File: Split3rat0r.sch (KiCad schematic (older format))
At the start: 69 parts, among them J1 Conn_01x20, K1 KEYSW, K10 KEYSW, K11 KEYSW, K12 KEYSW, K13 KEYSW, K14 KEYSW, K15 KEYSW, K16 KEYSW, K17 KEYSW, K18 KEYSW, K19 KEYSW, K2 KEYSW, K20 KEYSW, K21 KEYSW, K22 KEYSW, K23 KEYSW, K24 KEYSW, K25 KEYSW, K26 KEYSW, K27 KEYSW, K28 KEYSW, K29 KEYSW, K3 KEYSW, K30 KEYSW, K4 KEYSW, K5 KEYSW, K6 KEYSW, K7 KEYSW, K8 KEYSW, K9 KEYSW, U1 TEENSY2.0

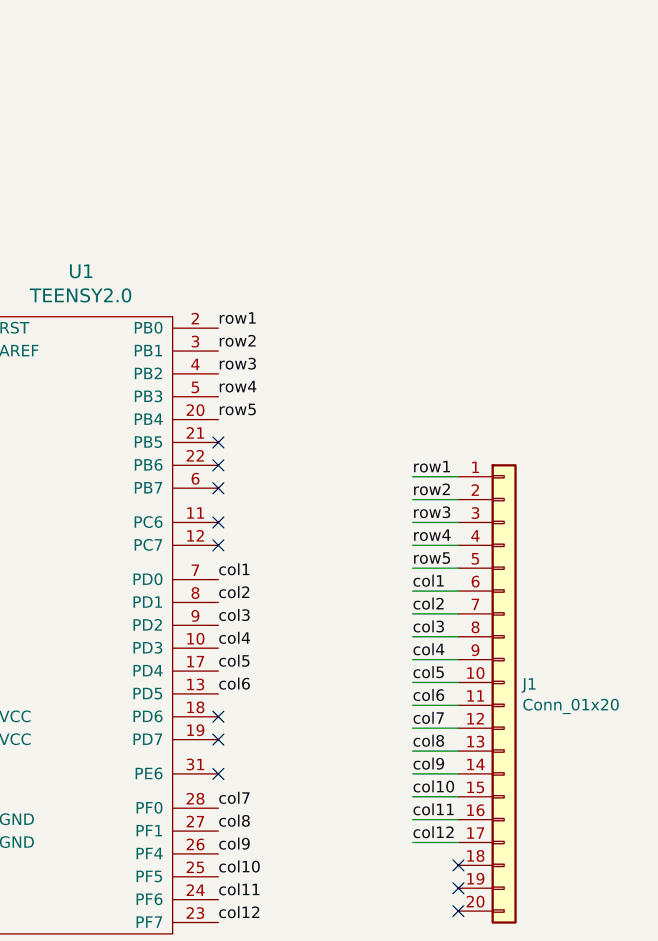
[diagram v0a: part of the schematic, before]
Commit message: Added LEDs beginning pcb layout
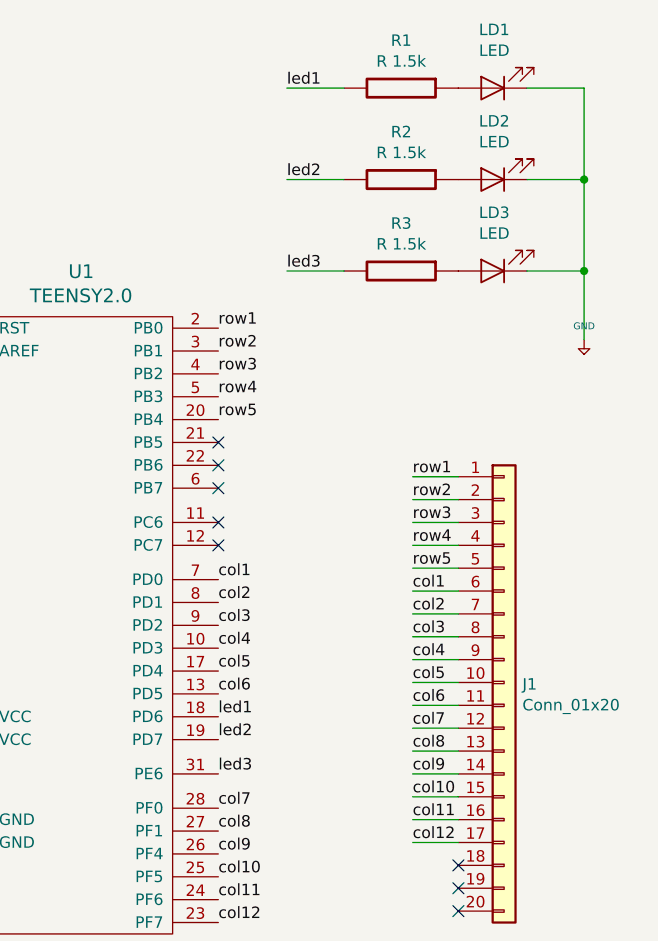
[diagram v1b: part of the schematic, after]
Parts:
- added LD1, LD2, LD3: LED, keeb_parts:LED_TH, symbol Device:LED
- added R1, R2, R3: R 1.5k, Resistor_THT:R_Axial_DIN0204_L3.6mm_D1.6mm_P5.08mm_Horizontal, symbol keeb_parts:R
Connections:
- net +5V: now also LD1.1 (K), LD2.1 (K), LD3.1 (K)
- net led1: now reaches U1.18 (PD6)
- net led1: now also R1.2
- net led2: now reaches U1.19 (PD7)
- net led2: now also R2.2
- net led3: now reaches U1.31 (PE6)
- net led3: now also R3.2
- new net: LD1.2 (A), R1.1
- new net: LD2.2 (A), R2.1
- new net: LD3.2 (A), R3.1
- no-connect marks 13 -> 10
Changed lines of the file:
@@
 NoConn ~ 8900 2850
 NoConn ~ 8900 2950
-NoConn ~ 8900 3700
-NoConn ~ 8900 3800
-NoConn ~ 8900 3950
 NoConn ~ 9950 4350
 NoConn ~ 9950 4450
@@
 	1    0    0    -1
 $EndComp
+$Comp
+L Device:LED LD1
+U 1 1 5CD186EE
+P 10100 950
+F 0 "LD1" H 10093 695 50  0000 C CNN
+F 1 "LED" H 10093 786 50  0000 C CNN
+F 2 "keeb_parts:LED_TH" H 10100 950 50  0001 C CNN
+F 3 "~" H 10100 950 50  0001 C CNN
+	1    10100 950
+	-1   0    0    1
+$EndComp
+$Comp
+L Device:LED LD2
+U 1 1 5CD19CA1
+P 10100 1350
+F 0 "LD2" H 10093 1095 50  0000 C CNN
+F 1 "LED" H 10093 1186 50  0000 C CNN
+F 2 "keeb_parts:LED_TH" H 10100 1350 50  0001 C CNN
+F 3 "~" H 10100 1350 50  0001 C CNN
+	1    10100 1350
+	-1   0    0    1
+$EndComp
+$Comp
+L Device:LED LD3
+U 1 1 5CD19E40
+P 10100 1750
+F 0 "LD3" H 10093 1495 50  0000 C CNN
+F 1 "LED" H 10093 1586 50  0000 C CNN
+F 2 "keeb_parts:LED_TH" H 10100 1750 50  0001 C CNN
+F 3 "~" H 10100 1750 50  0001 C CNN
+	1    10100 1750
+	-1   0    0    1
+$EndComp
+$Comp
+L keeb_parts:GND #PWR0105
+U 1 1 5CD1D128
+P 10500 2050
+F 0 "#PWR0105" H 10500 2100 20  0001 C CNN
+F 1 "GND" H 10500 2109 30  0000 C CNN
+F 2 "" H 10500 2050 60  0000 C CNN
+F 3 "" H 10500 2050 60  0000 C CNN
+	1    10500 2050
+	1    0    0    -1
+$EndComp
+Wire Wire Line
+	10250 1750 10500 1750
+Wire Wire Line
+	10500 1350 10250 1350
+Wire Wire Line
+	10250 950  10500 950
+Text Label 9200 950  0    50   ~ 0
+led1
+Text Label 9200 1350 0    50   ~ 0
+led2
+Text Label 9200 1750 0    50   ~ 0
+led3
+$Comp
+L keeb_parts:R R1
+U 1 1 5CD54691
+P 9700 950
+F 0 "R1" V 9492 950 50  0000 C CNN
+F 1 "R 1.5k" V 9583 950 50  0000 C CNN
+F 2 "Resistor_THT:R_Axial_DIN0204_L3.6mm_D1.6mm_P5.08mm_Horizontal" H 9700 950 60  0001 C CNN
+F 3 "" H 9700 950 60  0000 C CNN
+	1    9700 950
+	0    1    1    0
+$EndComp
+$Comp
+L keeb_parts:R R2
+U 1 1 5CD55293
+P 9700 1350
+F 0 "R2" V 9492 1350 50  0000 C CNN
+F 1 "R 1.5k" V 9583 1350 50  0000 C CNN
+F 2 "Resistor_THT:R_Axial_DIN0204_L3.6mm_D1.6mm_P5.08mm_Horizontal" H 9700 1350 60  0001 C CNN
+F 3 "" H 9700 1350 60  0000 C CNN
+	1    9700 1350
+	0    1    1    0
+$EndComp
+$Comp
+L keeb_parts:R R3
+U 1 1 5CD55692
+P 9700 1750
+F 0 "R3" V 9492 1750 50  0000 C CNN
+F 1 "R 1.5k" V 9583 1750 50  0000 C CNN
+F 2 "Resistor_THT:R_Axial_DIN0204_L3.6mm_D1.6mm_P5.08mm_Horizontal" H 9700 1750 60  0001 C CNN
+F 3 "" H 9700 1750 60  0000 C CNN
+	1    9700 1750
+	0    1    1    0
+$EndComp
+Wire Wire Line
+	9200 950  9450 950
+Wire Wire Line
+	9450 1350 9200 1350
+Wire Wire Line
+	9200 1750 9450 1750
+Wire Wire Line
+	10500 950  10500 1350
+Connection ~ 10500 1750
+Connection ~ 10500 1350
+Wire Wire Line
+	10500 1350 10500 1750
+Wire Wire Line
+	10500 1750 10500 2050
+Text Label 8900 3700 0    50   ~ 0
+led1
+Text Label 8900 3800 0    50   ~ 0
+led2
+Text Label 8900 3950 0    50   ~ 0
+led3
 $EndSCHEMATC

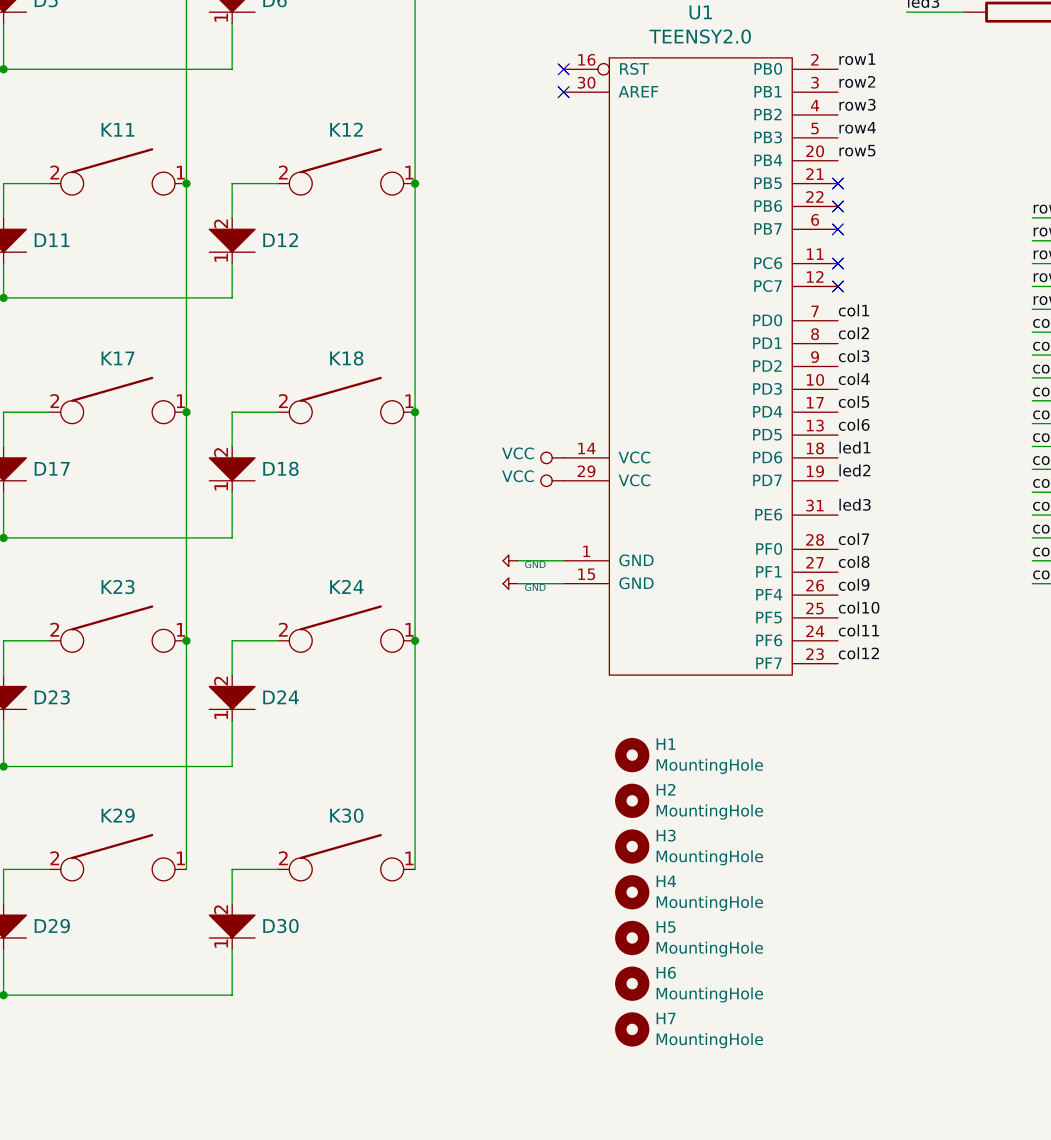
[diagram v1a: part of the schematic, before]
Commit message: Added rotary acoder switch + pcb layout progress
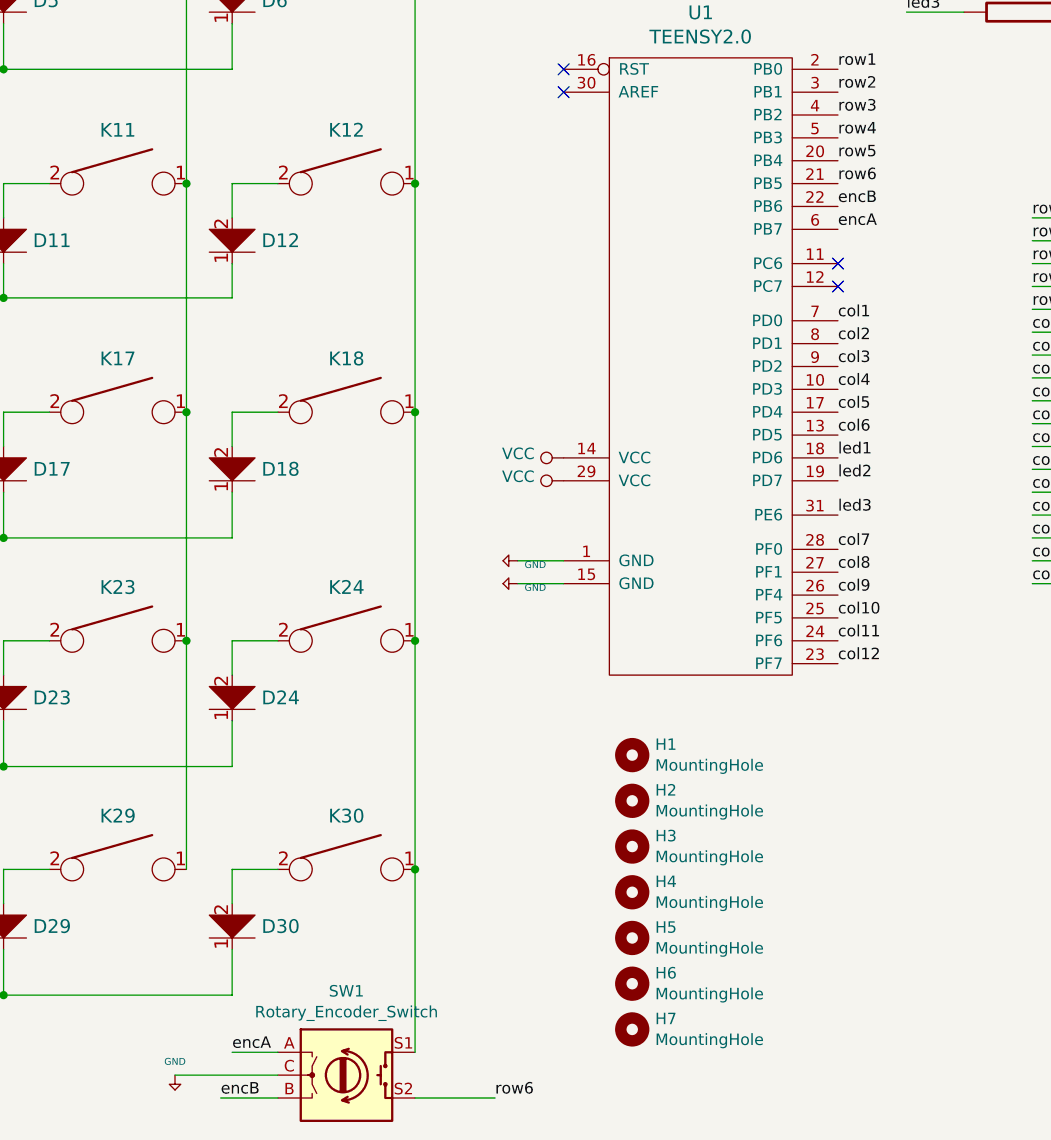
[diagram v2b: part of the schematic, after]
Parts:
- added SW1: Rotary_Encoder_Switch, Rotary_Encoder:RotaryEncoder_Alps_EC11E-Switch_Vertical_H20mm, symbol Device:Rotary_Encoder_Switch
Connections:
- net +5V: now also SW1.C
- net col6: now also SW1.S1
- net row6: now reaches U1.21 (PB5)
- net row6: now also SW1.S2
- net encB: now reaches U1.22 (PB6)
- net encB: now also SW1.B
- net encA: now reaches U1.6 (PB7)
- net encA: now also SW1.A
- no-connect marks 10 -> 7
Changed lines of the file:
@@
-$EndComp
-$Comp
-L keeb_parts:TEENSY2.0 U1
-U 1 1 5CD0FF01
-P 8300 3300
-F 0 "U1" H 8300 4847 60  0000 C CNN
-F 1 "TEENSY2.0" H 8300 4741 60  0000 C CNN
-F 2 "keeb:Teensy_20" H 8300 3300 60  0001 C CNN
-F 3 "" H 8300 3300 60  0000 C CNN
-	1    8300 3300
-	1    0    0    -1
 $EndComp
 $Comp
@@
 NoConn ~ 7700 2000
 NoConn ~ 7700 2100
-NoConn ~ 8900 2500
-NoConn ~ 8900 2600
-NoConn ~ 8900 2700
 NoConn ~ 8900 2850
 NoConn ~ 8900 2950
@@
 Text Label 8900 3950 0    50   ~ 0
 led3
+$Comp
+L keeb_parts:TEENSY2.0 U1
+U 1 1 5CD0FF01
+P 8300 3300
+F 0 "U1" H 8300 4847 60  0000 C CNN
+F 1 "TEENSY2.0" H 8300 4741 60  0000 C CNN
+F 2 "keeb:Teensy_20" H 8300 3300 60  0001 C CNN
+F 3 "" H 8300 3300 60  0000 C CNN
+	1    8300 3300
+	1    0    0    -1
+$EndComp
+$Comp
+L Device:Rotary_Encoder_Switch SW1
+U 1 1 5CD9B11F
+P 6750 6400
+F 0 "SW1" H 6750 6767 50  0000 C CNN
+F 1 "Rotary_Encoder_Switch" H 6750 6676 50  0000 C CNN
+F 2 "Rotary_Encoder:RotaryEncoder_Alps_EC11E-Switch_Vertical_H20mm" H 6600 6560 50  0001 C CNN
+F 3 "~" H 6750 6660 50  0001 C CNN
+	1    6750 6400
+	1    0    0    -1
+$EndComp
+Connection ~ 7050 5500
+Wire Wire Line
+	7050 5500 7050 6300
+Wire Wire Line
+	7050 6500 7400 6500
+Text Label 7400 6500 0    50   ~ 0
+row6
+Wire Wire Line
+	6450 6400 6000 6400
+$Comp
+L keeb_parts:GND #PWR?
+U 1 1 5CDF87FD
+P 6000 6400
+F 0 "#PWR?" H 6000 6450 20  0001 C CNN
+F 1 "GND" H 6000 6459 30  0000 C CNN
+F 2 "" H 6000 6400 60  0000 C CNN
+F 3 "" H 6000 6400 60  0000 C CNN
+	1    6000 6400
+	1    0    0    -1
+$EndComp
+Wire Wire Line
+	6450 6300 6250 6300
+Wire Wire Line
+	6450 6500 6200 6500
+Text Label 6200 6500 0    50   ~ 0
+encB
+Text Label 6250 6300 0    50   ~ 0
+encA
+Text Label 8900 2500 0    50   ~ 0
+row6
+Text Label 8900 2600 0    50   ~ 0
+encB
+Text Label 8900 2700 0    50   ~ 0
+encA
 $EndSCHEMATC
